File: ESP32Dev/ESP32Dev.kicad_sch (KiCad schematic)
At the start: 31 parts, among them J1 Conn, SW1 Reset, SW2 Boot, U1 ESP32-WROOM-32, U2 AP1117-33

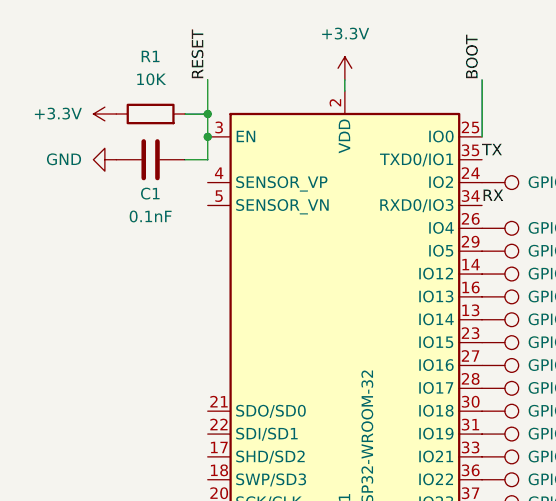
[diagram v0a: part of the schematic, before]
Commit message: ESP32: Fixed capacitor value
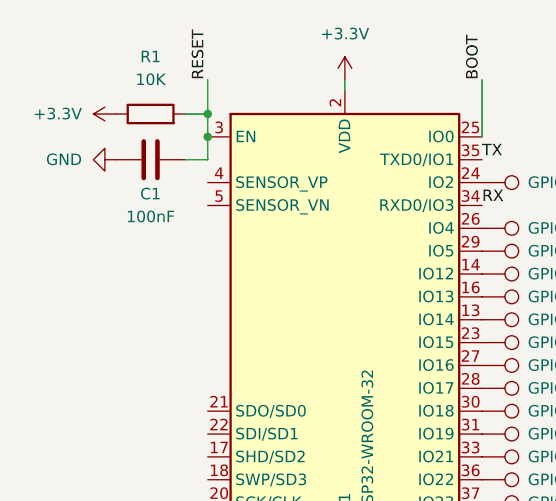
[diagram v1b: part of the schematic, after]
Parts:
- C1: value 0.1nF -> 100nF
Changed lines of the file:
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@@
     (in_bom yes) (on_board yes)
     (property "Reference" "C1" (id 0) (at 85.09 78.74 90))
-    (property "Value" "0.1nF" (id 1) (at 85.09 81.28 90))
+    (property "Value" "100nF" (id 1) (at 85.09 81.28 90))
     (property "Footprint" "Capacitor_SMD:C_1206_3216Metric_Pad1.33x1.80mm_HandSolder" (id 2) (at 88.9 73.9648 0)
       (effects (font (size 1.27 1.27)) hide)
@@
     )
     (path "/a04260aa-8b62-4cfd-8ce8-f7c7cbc3ff88"
-      (reference "C1") (unit 1) (value "0.1nF") (footprint "Capacitor_SMD:C_1206_3216Metric_Pad1.33x1.80mm_HandSolder")
+      (reference "C1") (unit 1) (value "100nF") (footprint "Capacitor_SMD:C_1206_3216Metric_Pad1.33x1.80mm_HandSolder")
     )
     (path "/2fe94878-74ec-4c50-86a4-23fada804b38"
